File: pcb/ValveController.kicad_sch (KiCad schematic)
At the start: 48 parts, among them J10 1770966, J11 1770966, J12 1770966, J13 USB4105-GF-A, J2 1990986, J3 1990986, J8 1770966, J9 1770966, Q3 MOC3063S-TA1, Q4 MOC3063S-TA1, SW1 TL9320AF400QG, U1 IRM-03-5, U2 TLV75733P, U5 ESP32-C6-WROOM-1-N4

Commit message: chore(pcb): reorganize into pcb/ and consolidate 3D models
Move the KiCad project into pcb/, flatten custom STEP models into pcb/3dmodels/ (rewriting the KIPRJMOD-relative model paths in the board and footprints), relocate manual .bak snapshots to git-ignored pcb/backups/, and drop regenerable gerber outputs. Restore .gitignore.
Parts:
- added H1, H2: MountingHole, MountingHole:MountingHole_3.2mm_M3_DIN965_Pad, symbol Mechanical:MountingHole
- added H3, H4: MountingHole, MountingHole:MountingHole_3.2mm_M3_DIN965_Pad, symbol Mechanical:MountingHole_Pad
- added R8, R9: 10k, Resistor_SMD:R_0402_1005Metric, symbol R_dev
- CS1, CS2: value 100nF X2 -> 22nF X2; DigiKey https://www.digikey.com/en/products/detail/epcos-tdk-electr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 -> https://www.digikey.com/en/products/detail/kemet/R463I22204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; MPN B32922C3104M000 -> R463I22204001M
- D1: value LED -> LED (active-low)
- J13: value USB4105-GF-A -> USB4115-03-C; DigiKey https://www.digikey.com/en/products/detail/gct/USB4105-GF-A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 -> https://www.digikey.nl/nl/products/detail/gct/USB4115-03-C/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; MPN USB4105-GF-A -> USB4115-03-C
- RL1, RL2: value 330 -> 180; DigiKey https://www.digikey.com/en/products/detail/yageo/RC0402FR-07330RL/726594 -> https://www.digikey.com/en/products/detail/yageo/RC0402FR-07180RL/726550; MPN RC0402FR-07330RL -> RC0402FR-07180RL
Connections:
- net 3V3: now also R4.1
- net GND: now also H3.1, H4.1, R8.2, R9.2; no longer D1.2
- net LED_A: now also D1.2; no longer D1.1
- net SSR_CLOSE: now also R9.1
- net SSR_OPEN: now also R8.1
- net STAT_LED: now also D1.1; no longer R4.1
- net DBG_RX: no longer names the net of U5.24 (RXD0)
- net DBG_TX: no longer names the net of U5.25 (TXD0)
- no-connect marks 6 -> 17
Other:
- moved on the sheet: SW1

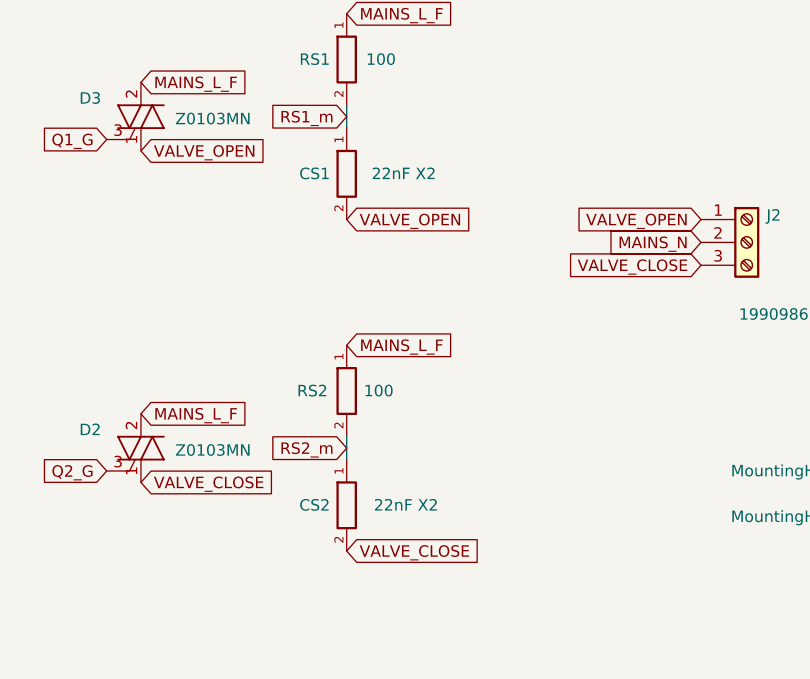
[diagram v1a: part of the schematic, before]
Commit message: fix(pcb): CS1/CS2 snubber 22nF X2 -> 4.7nF X1 (ECQ-UBAF472V5, actuator hum)
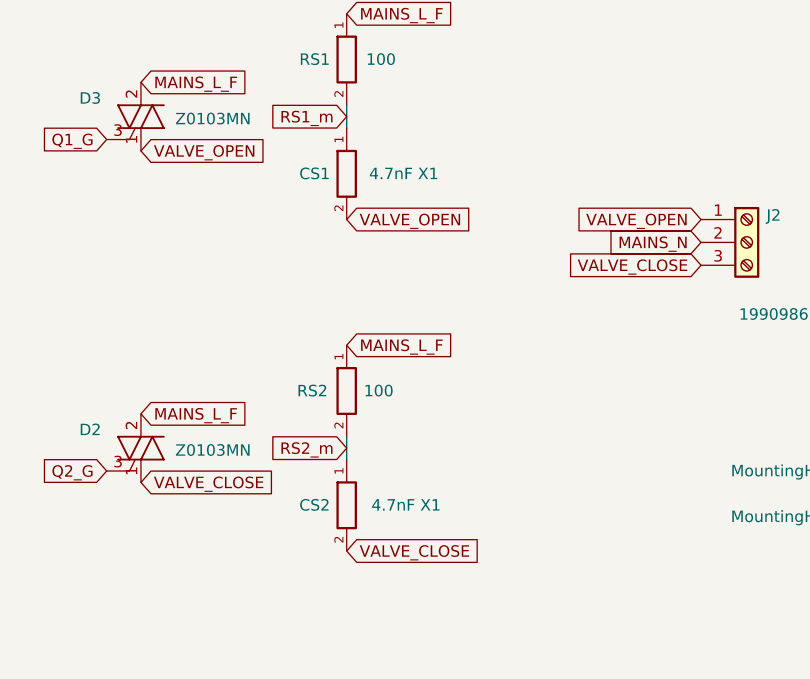
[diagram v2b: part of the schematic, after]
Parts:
- CS1, CS2: value 22nF X2 -> 4.7nF X1; DigiKey https://www.digikey.com/en/products/detail/kemet/R463I22204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 -> https://www.digikey.nl/nl/products/detail/panasonic-industr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; MPN R463I22204001M -> ECQ-UBAF472V5
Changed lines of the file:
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@@
 			)
 		)
-		(property "Value" "22nF X2"
+		(property "Value" "4.7nF X1"
 			(at 161.544 166.37 0)
 			(show_name no)
@@
 			)
 		)
-		(property "MPN" "R463I22204001M"
+		(property "MPN" "ECQ-UBAF472V5"
 			(at 154.94 166.37 0)
 			(hide yes)
@@
 			)
 		)
-		(property "DigiKey" "https://www.digikey.com/en/products/detail/kemet/R463I22204001M/9561553"
+		(property "DigiKey" "https://www.digikey.nl/nl/products/detail/panasonic-industry/ECQ-UBAF472V5/13280231"
 			(at 154.94 166.37 0)
 			(hide yes)
@@
 			)
 		)
-		(property "Value" "22nF X2"
+		(property "Value" "4.7nF X1"
 			(at 161.29 129.54 0)
 			(show_name no)
@@
 			)
 		)
-		(property "MPN" "R463I22204001M"
+		(property "MPN" "ECQ-UBAF472V5"
 			(at 154.94 129.54 0)
 			(hide yes)
@@
 			)
 		)
-		(property "DigiKey" "https://www.digikey.com/en/products/detail/kemet/R463I22204001M/9561553"
+		(property "DigiKey" "https://www.digikey.nl/nl/products/detail/panasonic-industry/ECQ-UBAF472V5/13280231"
 			(at 154.94 129.54 0)
 			(hide yes)

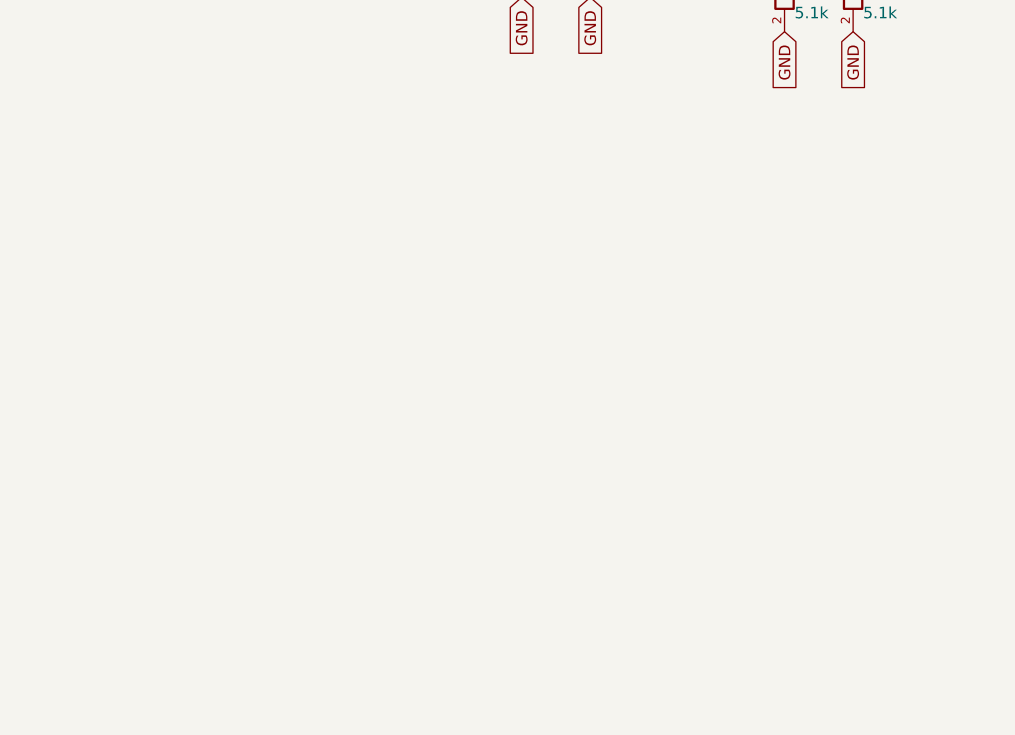
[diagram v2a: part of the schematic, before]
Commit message: feat(pcb): 24V boost leaf (TPS61040) for pump iPWM interface
Add TPS61040DRVR (WSON-6) 5V->24V boost converter block for the Wilo
Para ST 15-7-50 iPWM2 drive input: U6 (TPS61040DRVR), L1 (10uH boost
inductor), D6 (B5819W rectifier), C9 (input cap), C10/C11 (output
caps), R10/R11 (1M/53.6k FB divider, Vout~=24.2V), C13 (22pF
feedforward cap across R10 per TI datasheet reference design).

New nets: 24V, 24V_SW, 24V_FB. Grows 5V and GND per plan. U6 pin 5
(NC) explicitly flagged with a no-connect marker.

ERC: zero new errors, zero new violation categories; +8 warnings are
all pre-existing lib_symbol_issues (one per new R_dev/C_dev/L_dev/
Kleist-style symbol, matching every other passive already on this
sheet). Netlist diff verified against baseline: exact match to the
planned net-membership delta, no unexplained changes.
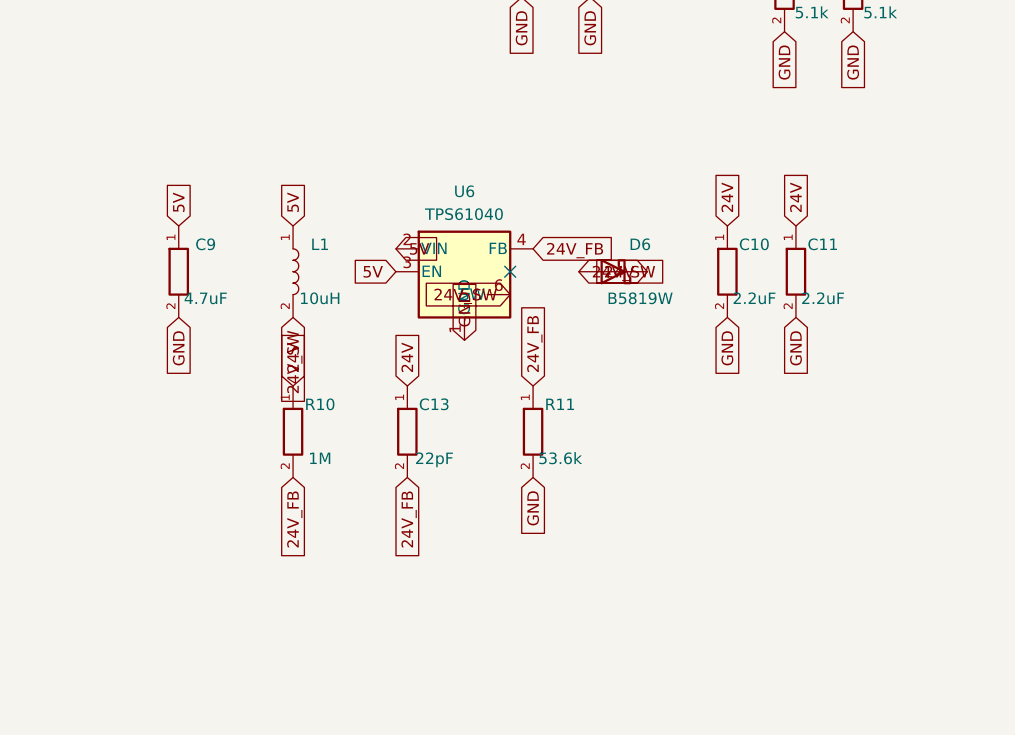
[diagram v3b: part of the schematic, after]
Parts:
- added C10, C11: 2.2uF, Capacitor_SMD:C_1206_3216Metric, symbol C_dev
- added C13: 22pF, Capacitor_SMD:C_0402_1005Metric, symbol C_dev
- added C9: 4.7uF, Capacitor_SMD:C_0805_2012Metric, symbol C_dev
- added D6: B5819W, Diode_SMD:D_SOD-123, symbol Device:D_Schottky
- added L1: 10uH, Inductor_SMD:L_Taiyo-Yuden_NR-40xx, symbol L_dev
- added R10: 1M, Resistor_SMD:R_0402_1005Metric, symbol R_dev
- added R11: 53.6k, Resistor_SMD:R_0402_1005Metric, symbol R_dev
- added U6: TPS61040, Package_SON:WSON-6-1EP_2x2mm_P0.65mm_EP1x1.6mm_ThermalVias, symbol Kleist:TPS61040DRV
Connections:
- net 5V: now also C9.1, L1.1, U6.2 (VIN), U6.3 (EN)
- net GND: now also C10.2, C11.2, C9.2, R11.2, U6.1 (GND), U6.7 (GND)
- new net 24V: C10.1, C11.1, C13.1, D6.1 (K), R10.1
- new net 24V_FB: C13.2, R10.2, R11.1, U6.4 (FB)
- new net 24V_SW: D6.2 (A), L1.2, U6.6 (SW)
- no-connect marks 17 -> 18

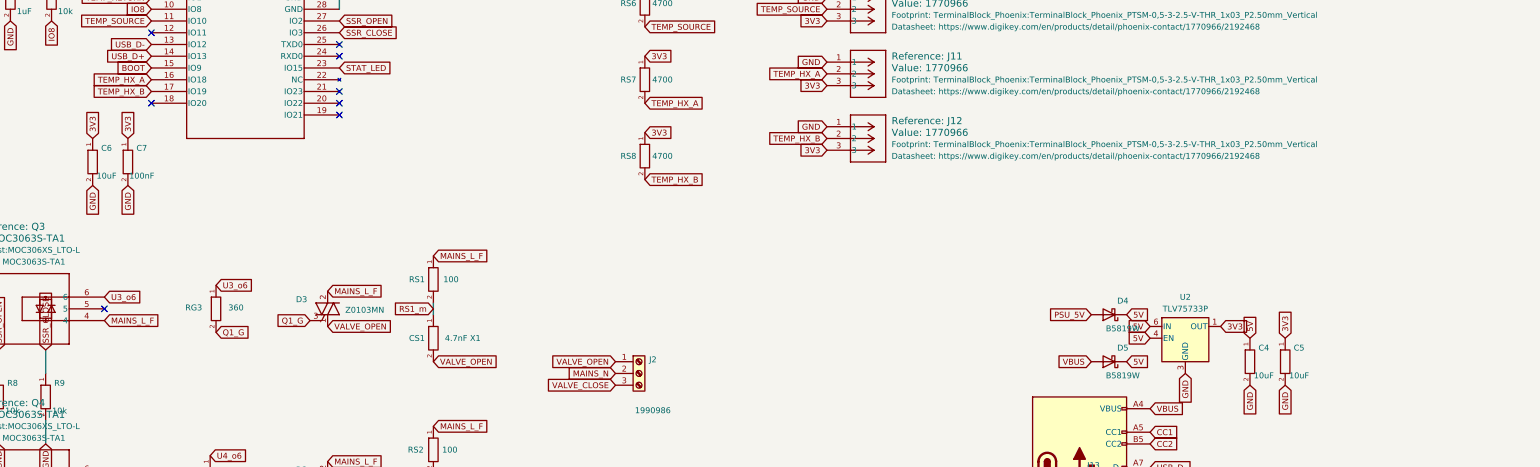
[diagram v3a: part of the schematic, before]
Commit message: feat(pcb): iPWM2 pump drive, feedback conditioning, J14 (Wilo core order)
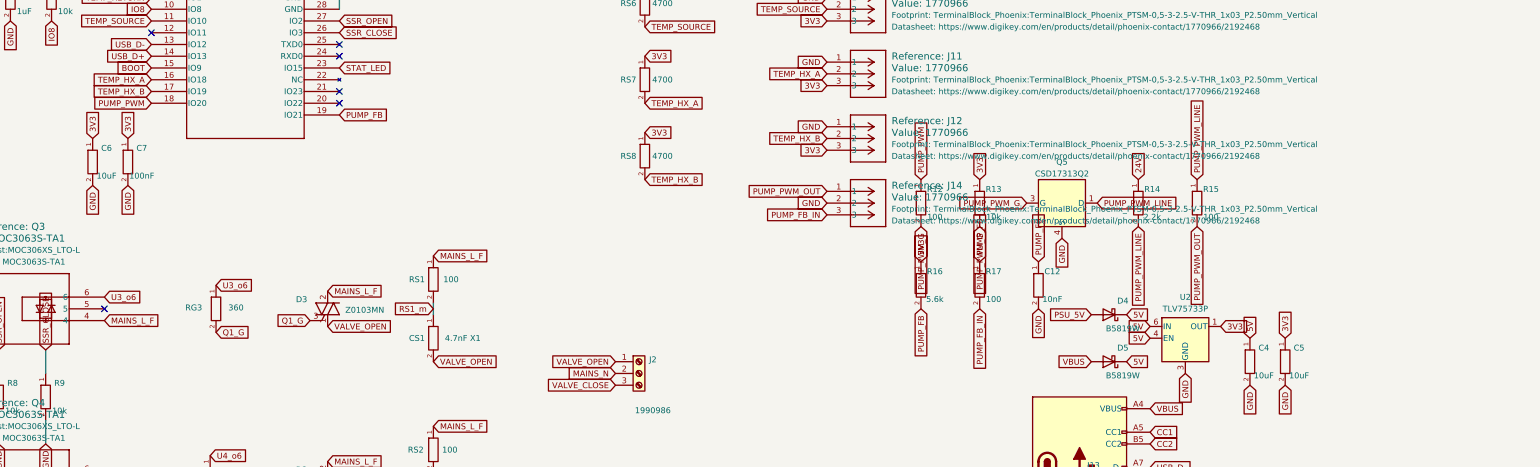
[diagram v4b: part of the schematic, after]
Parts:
- added C12: 10nF, Capacitor_SMD:C_0402_1005Metric, symbol C_dev
- added J14: 1770966, TerminalBlock_Phoenix:TerminalBlock_Phoenix_PTSM-0,5-3-2.5-V-THR_1x03_P2.50mm_Vertical, symbol Kleist:901361103
- added Q5: CSD17313Q2, Kleist2:CSD17313Q2, symbol Kleist:CSD17313Q2
- added R12: 100, Resistor_SMD:R_0402_1005Metric, symbol R_dev
- added R13: 10k, Resistor_SMD:R_0402_1005Metric, symbol R_dev
- added R14: 2.2k, Resistor_SMD:R_1206_3216Metric, symbol R_dev
- added R15, R17: 100, Resistor_SMD:R_1206_3216Metric, symbol R_dev
- added R16: 5.6k, Resistor_SMD:R_0402_1005Metric, symbol R_dev
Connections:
- net 24V: now also R14.1
- net 3V3: now also R13.1, R16.1
- net GND: now also C12.2, J14.2, Q5.4 (S), Q5.7 (EP)
- net PUMP_PWM: now reaches U5.18 (IO20)
- net PUMP_PWM: now also R12.1
- net PUMP_FB: now reaches U5.19 (IO21)
- net PUMP_FB: now also C12.1, R16.2, R17.1
- new net PUMP_FB_IN: J14.3, R17.2
- new net PUMP_PWM_G: Q5.3 (G), R12.2, R13.2
- new net PUMP_PWM_LINE: Q5.1 (D), Q5.2 (D), Q5.5 (D), Q5.6 (D), Q5.8 (D), R14.2, R15.1
- new net PUMP_PWM_OUT: J14.1, R15.2
- no-connect marks 18 -> 16
